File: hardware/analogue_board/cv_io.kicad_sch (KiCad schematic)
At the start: 55 parts, among them J401 CV jack holes, U401 ADS8688IDBTR, U402 DG412DQ-T1-E3, U403 DG412DQ-T1-E3

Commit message: Analogue board: block review applied, TRS MIDI, ESP32-P4 support
Checkpoint 1 schematic rebuilt after a block-by-block prior-art review
(docs/analogue_board_review/, seven reports and an index).

Schematic:
- Codec: 20 Vpp in and out (15k input feedback; balanced MFB output,
  gain 2.5, 1 nF C0G); ferrite and 5.1 ohm on the codec supplies; VCOM
  decoupled at each input; CODEC_RST to a hole.
- Power: 680 ohm minimum load on +3V3D; buck input ferrite and EN
  divider; SS34 at D201-D203; Q201/JP201 MOD_5V bypass for the ESP32-P4.
- CV in: 15 V TVS at each jack, 1 nF at each ADC input, 1206 outputs.
- CV out: 12k/22k offset with 1 nF, 33k gain; CV7-8 feedback from the
  jack side of the 1k.
- Gates and panel: CS_595 pull-up, GATE_OE_N on J603, 1M wiper
  pull-downs, POT_REF, button RC order, 47 uF at the LED holes.
- New sheet 10: TRS MIDI (Type A), H11L1 in, 5 V buffered out.
- Layout: no overlapping text on any sheet.

ERC 0/0; netlist identical to intent (345 nets); 21 ICs against
datasheets; 17 Extended part types.

Spec v0.4: David's decisions (TVS yes, CV +/-5 V with a +/-10 V
variant, ESP32-P4 accommodated, power header free to move), the
corrections, and a firmware requirements list in section 15.

Co-Authored-By: Claude Opus 5.5 <noreply@anthropic.com>
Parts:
- removed C409: 100n 50V, Capacitor_SMD:C_0603_1608Metric, symbol Device:C_Small
- removed C411: 100n 16V, Capacitor_SMD:C_0402_1005Metric, symbol Device:C_Small
- removed R408, R412: 100k, Resistor_SMD:R_0402_1005Metric, symbol Device:R_Small
- removed R432: 1k, Resistor_SMD:R_0402_1005Metric, symbol Device:R_Small
- added C415, C416: 1n 50V, Capacitor_SMD:C_0402_1005Metric, symbol Device:C_Small
- added C417, C418, C420, C421: 100n 50V, Capacitor_SMD:C_0603_1608Metric, symbol Device:C_Small
- added C419, C422: 100n 16V, Capacitor_SMD:C_0402_1005Metric, symbol Device:C_Small
- added D401, D402, D403, D404, D405, D406, D407, D408: PESD15VL1BA, Diode_SMD:D_SOD-323, symbol Device:D_TVS
- added R405, R421: 100k, Resistor_SMD:R_0402_1005Metric, symbol Device:R_Small
- added R410: 1k, Resistor_SMD:R_1206_3216Metric, symbol Device:R_Small
- added unit 2 of U402
- C409: renamed from R405; value 1k -> 1n 50V; footprint Resistor_SMD:R_0402_1005Metric -> Capacitor_SMD:C_0402_1005Metric; symbol Device:R_Small -> Device:C_Small; Dielectric (none) -> X7R; LCSC C11702 -> C1523; Note (none) -> RF/ESD filter at the ADC pin (TI EVM); Tolerance 1% -> (none); Voltage (none) -> 50V
- C410: value 100n 50V -> 1n 50V; footprint Capacitor_SMD:C_0603_1608Metric -> Capacitor_SMD:C_0402_1005Metric; Decouples U402 V- pin 4 -> (none); LCSC C14663 -> C1523; Note (none) -> RF/ESD filter at the ADC pin (TI EVM)
- C411: renamed from U402; value DG412DQ-T1-E3 -> 1n 50V; footprint Package_SO:TSSOP-16_4.4x5mm_P0.65mm -> Capacitor_SMD:C_0402_1005Metric; symbol Analog_Switch:DG412xUE -> Device:C_Small; Dielectric (none) -> X7R; JLC Extended -> Basic; LCSC C2651920 -> C1523; MPN DG412DQ-T1-E3 -> (none); Note (none) -> RF/ESD filter at the ADC pin (TI EVM); Voltage (none) -> 50V
- C412: value 100n 50V -> 1n 50V; footprint Capacitor_SMD:C_0603_1608Metric -> Capacitor_SMD:C_0402_1005Metric; Decouples U403 V+ pin 13 -> (none); LCSC C14663 -> C1523; Note (none) -> RF/ESD filter at the ADC pin (TI EVM)
- C413: value 100n 50V -> 1n 50V; footprint Capacitor_SMD:C_0603_1608Metric -> Capacitor_SMD:C_0402_1005Metric; Decouples U403 V- pin 4 -> (none); LCSC C14663 -> C1523; Note (none) -> RF/ESD filter at the ADC pin (TI EVM)
- C414: value 100n 16V -> 1n 50V; Decouples U403 VL pin 12 -> (none); LCSC C1525 -> C1523; Note (none) -> RF/ESD filter at the ADC pin (TI EVM); Voltage 16V -> 50V
- R403: value 1k -> 10k; LCSC C11702 -> C25744; Note (none) -> AVDD below 30 kΩ when unpowered: keeps the ±20 V OVP rating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
- R404, R420, R424, R428, R430: value 100k -> 1k; LCSC C25741 -> C11702
- R406, R414, R418, R422, R426: value 4.7k -> 1k; footprint Resistor_SMD:R_0402_1005Metric -> Resistor_SMD:R_1206_3216Metric; LCSC C25900 -> C4410; Note beats the TCA9555 internal pull-up -> 1206: survives output-to-output patching
- R407, R411, R415, R419, R423, R427: value 1k -> 4.7k; LCSC C11702 -> C25900; Note (none) -> beats the TCA9555 internal pull-up
- R408: renamed from R410; value 4.7k -> 1k; LCSC C25900 -> C11702; Note beats the TCA9555 internal pull-up -> (none)
- R409, R413, R417, R425, R429, R431: value 1k -> 100k; LCSC C11702 -> C25741
- R412: renamed from R416; value 100k -> 1k; LCSC C25741 -> C11702
- renumbered R421 to R416
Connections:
- net CVDRV7 is gone; now on net ADC_IN8: R431.1
- net +12V: now also C417.1, C420.1; no longer C412.1
- net +5VA: now also R403.1
- net +5VD: now also C419.1, C422.1; no longer C414.1
- net -12V: now also C418.1, C421.1; no longer C410.1, C413.1
- net ADC_IN1: now also C409.1, R404.2, R405.1; no longer R403.2, R404.1
- net ADC_IN2: now also C410.1, R408.2, R409.1; no longer R407.2
- net ADC_IN3: now also C411.1, R412.2, R413.1; no longer R411.2
- net ADC_IN4: now also C412.1, R416.2, R417.1; no longer R412.1, R415.2
- net ADC_IN5: now also C413.1, R420.2, R421.1; no longer R419.2, R420.1
- net ADC_IN6: now also C414.1, R424.2, R425.1; no longer R423.2, R424.1
- net ADC_IN7: now also R428.2, R429.1, C415.1; no longer R427.2, R428.1
- net ADC_IN8: now also R430.2, C416.1; no longer R429.2, R430.1
- net CV1: now also R404.1, R406.2, D401.2 (A2); no longer C409.2, R403.1
- net CV2: now also R408.1, D402.2 (A2), R410.2; no longer R407.1, R409.2
- net CV3: now also R412.1, R414.2, D403.2 (A2); no longer R411.1, R413.2
- net CV4: now also R416.1, R418.2, D404.2 (A2); no longer R415.1, R417.2
- net CV5: now also R420.1, R422.2, D405.2 (A2); no longer R416.2, R419.1
- net CV6: now also R424.1, R426.2, D406.2 (A2); no longer R423.1, R425.2
- net CVDRV4: now also U402.7; no longer C411.7
- net CVI7: now also R428.1, D407.2 (A2); no longer R427.1
- net CVI8: now also R430.1, D408.2 (A2); no longer R429.1
- net CVO7: no longer R431.2
- net GND: now also C409.2, C411.2, R403.2, R407.2, R409.2, R411.2, R413.2, R415.2, R417.2, R419.2, R423.2, R425.2, R427.2, R429.2, R431.2, C415.2, C416.2, C417.2, C418.2, C419.2, C420.2, C421.2, C422.2, D401.1 (A1), D402.1 (A1), D403.1 (A1), D404.1 (A1), D405.1 (A1), D406.1 (A1), D407.1 (A1), D408.1 (A1), R405.2, R421.2; no longer R404.2, R406.2, R408.2, R412.2, R414.2, R418.2, R420.2, R422.2, R424.2, R426.2, R428.2, R430.2
- net SW_EN1: now also R407.1; no longer R406.1
- net SW_EN2: now also R411.1; no longer R408.1
- net SW_EN3: now also R415.1; no longer R414.1
- net SW_EN4: now also R419.1, U402.8; no longer C411.8, R418.1
- net SW_EN5: now also R423.1; no longer R422.1
- net SW_EN6: now also R427.1; no longer R426.1
- net at U402.2: now also R406.1; no longer C409.1
- net at U403.2: now also R422.1; no longer R416.1
- net at U402.15: now also R410.1; no longer R409.1
- net at U402.10: now also R414.1; no longer R413.1
- net at U403.15: now also R426.1; no longer R425.1
- new net: R418.1, U402.6
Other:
- note added: "ADS8688: 8 channels, 16-bit, 1 MΩ inputs with ±10.24 / ±5.12 V ranges per channel (firmware default ±10.24 V), OVP ±20 V. Each CV jack: 15 V TVS at the hole, read through 1 kΩ with 1 nF at the ADC pin (TI's EVM). 100 kΩ to ground, but the ADC's 1 MΩ returns to an internal bias, so an UNPATCHED input reads ≈ +0.2 V: firmware trusts the jack-detect probe. CV1-6 are bidirectional: a DG412 switch (on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"
- note added: "CVO7, CVO8 (out only): their 1 kΩ sits inside the DAC stage's feedback loop on the CV DAC sheet, so the jack holds its voltage under load. Calibrate them with a cable to CVI7 / CVI8."
- note removed: "ADS8688: 8 channels, 16-bit, 1 MΩ inputs with ±10.24 / ±5.12 V ranges set per channel in firmware, OVP ±20 V. Every CV jack is read through 1 kΩ; 100 kΩ holds an unpatched input at 0 V. CV1-6 are bidirectional: a DG412 switch (on at logic 1) joins the DAC stage to the jack through another 1 kΩ, so with the switch on the ADC reads the jack itself. The TCA9555 lines have internal pull-ups, so each 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"
- note removed: "CV7, CV8 out only: DAC stage → 1 kΩ → jack"
- moved on the sheet: R403, R408, R412, R416

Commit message: Analogue board: checkpoint 3 started; double-sided, floorplan placed
- pcb.py generates analogue_board.kicad_pcb from the netlist: outline,
  JLC 4-layer stack-up, every footprint with nets and schematic links
  (KiCad schematic parity: 0 differences), parked parts beside the board,
  courtyard area budget, DRC and 3D renders of both faces.
- Area budget: the courtyards need 104% of one face before routing, so
  David chose double-sided assembly (JLC Standard PCBA, about $100 more
  per order, to confirm on a quote).
- Floorplan in placement.py: analogue ICs at the top under the modules,
  furthest from the buck; logic below; power bottom right around J201;
  MIDI bottom left; 99 wiring-field holes in three columns lined up with
  the edge-strip positions, each group beside its circuit.
- Library: module socket courtyards cover only their header rows; the
  wiring holes get their own footprint with a one-pitch courtyard.
- Spec records the decision, the floorplan and David's answers: 11 mm to
  the deck in 10HP (deck parts 2 mm at most); holes tinned both faces.

Co-Authored-By: Claude Opus 5.5 <noreply@anthropic.com>
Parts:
- J401: footprint Connector_PinHeader_2.54mm:PinHeader_1x12_P2.54mm_Vertical -> analogue_board:WiringHoles_1x12
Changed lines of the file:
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@@
 			)
 		)
-		(property "Footprint" "Connector_PinHeader_2.54mm:PinHeader_1x12_P2.54mm_Vertical"
+		(property "Footprint" "analogue_board:WiringHoles_1x12"
 			(at 350.52 165.1 0)
 			(effects

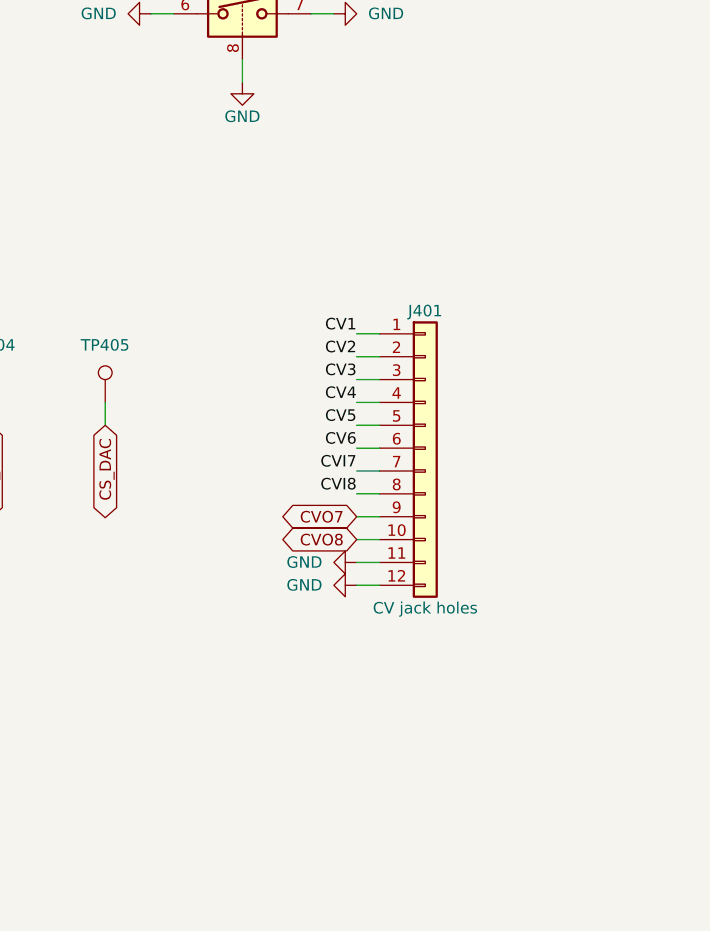
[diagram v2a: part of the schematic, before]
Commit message: Analogue board: first-pass placement; space reclaimed; four wiring banks
- autoplace.py places every unanchored part as close as it fits to the
  pins it connects to: decoupling capacitors at their pin, chains growing
  from their ICs, the buck's loop kept on one face. All 430 parts placed;
  DRC courtyards clean, schematic parity clean, heights checked (<= 2.5 mm
  under the modules, <= 8 mm in the USB keep-outs).
- Space reclaimed (David): Teensy socket without holes for its unused
  far-end pins 20-28 (headers 1x19 + 1x20); right strip (10HP only) without
  holes at 11-15 and 26-30, and outer hole only at 10, 16, 31. checks.py
  lets a project footprint omit only pins the netlist leaves unconnected.
- 74HCT595 in TSSOP-16 (74HCT595PW, C99710, same pinout) sideways in the
  right channel; vertical Qwiic socket (BM04B-SRSS-TB, C160390) below the
  modules, its cable straight up (the side-entry plug had no clear run).
- Wiring field as four mixed banks (David): each quarter of the board has
  some of every channel type, 50/50 left and right, jack-detect holes
  beside their inputs; wiring.py holds the plan, schematic and placement
  both read it. 94 holes.
- Reference designators off the silkscreen for passives and hole groups.

Co-Authored-By: Claude Opus 5.5 <noreply@anthropic.com>
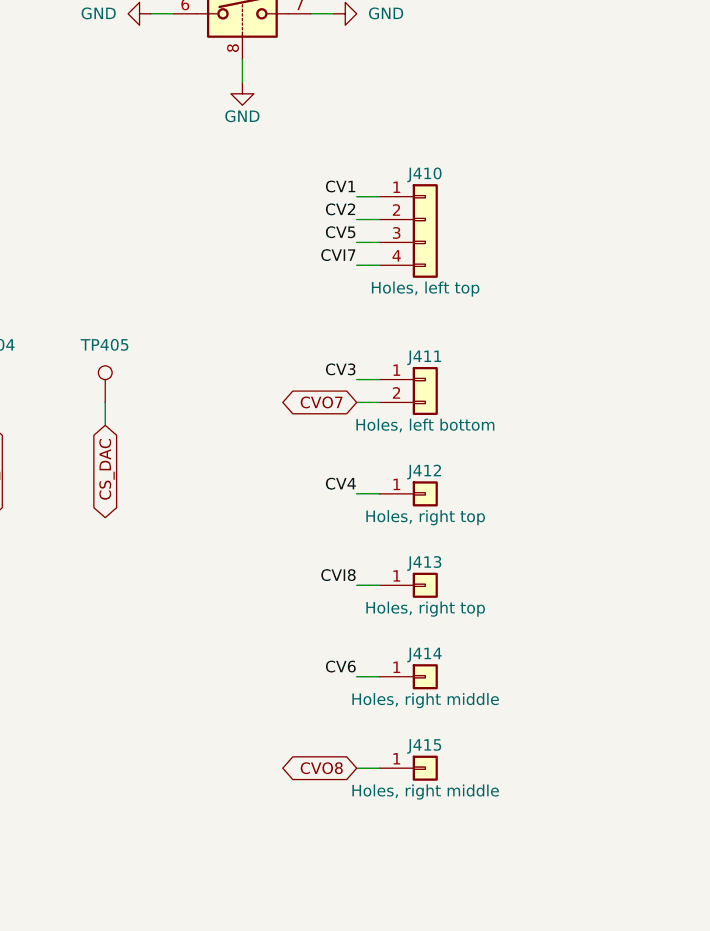
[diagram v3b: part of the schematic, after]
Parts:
- added J411: Holes, left bottom, analogue_board:WiringHoles_1x02, symbol Connector_Generic:Conn_01x02
- added J412, J413: Holes, right top, analogue_board:WiringHoles_1x01, symbol Connector_Generic:Conn_01x01
- added J414, J415: Holes, right middle, analogue_board:WiringHoles_1x01, symbol Connector_Generic:Conn_01x01
- J410: renamed from J401; value CV jack holes -> Holes, left top; footprint analogue_board:WiringHoles_1x12 -> analogue_board:WiringHoles_1x04; symbol Connector_Generic:Conn_01x12 -> Connector_Generic:Conn_01x04
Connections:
- net CV3: now also J411.1 (Pin_1); no longer J410.3 (Pin_3)
- net CV4: now also J412.1 (Pin_1); no longer J410.4 (Pin_4)
- net CV5: now also J410.3 (Pin_3); no longer J410.5 (Pin_5)
- net CV6: now also J414.1 (Pin_1); no longer J410.6 (Pin_6)
- net CVI7: now also J410.4 (Pin_4); no longer J410.7 (Pin_7)
- net CVI8: now also J413.1 (Pin_1); no longer J410.8 (Pin_8)
- net CVO7: now also J411.2 (Pin_2); no longer J410.9 (Pin_9)
- net CVO8: now also J415.1 (Pin_1); no longer J410.10 (Pin_10)
- net GND: no longer J410.11 (Pin_11), J410.12 (Pin_12)
